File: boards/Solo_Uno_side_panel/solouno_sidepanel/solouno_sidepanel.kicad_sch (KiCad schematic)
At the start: 1 part, among them J1 Conn_01x02

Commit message: Add files via upload
Updated Solo uno board
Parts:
- added A1: Aviation Connector, Library:GX-16-3, symbol Connector:DIN-3
- added A2: Aviation Pin, Connector_PinHeader_2.54mm:PinHeader_1x03_P2.54mm_Vertical, symbol Connector_Generic:Conn_01x03
- added C1: 3.3uF, Capacitor_THT:CP_Radial_D4.0mm_P1.50mm, symbol Device:C
- added CN1: CAN Front, Connector_PinHeader_2.54mm:PinHeader_1x02_P2.54mm_Vertical, symbol Connector_Generic:Conn_01x02
- added CN2: CAN Back, Connector_PinHeader_2.54mm:PinHeader_1x02_P2.54mm_Vertical, symbol Connector_Generic:Conn_01x02
- added E1: Encoder Front, Connector_PinHeader_2.54mm:PinHeader_1x05_P2.54mm_Vertical, symbol Connector_Generic:Conn_01x05
- added E2: Encoder Back, Connector_PinHeader_2.54mm:PinHeader_1x05_P2.54mm_Vertical, symbol Connector_Generic:Conn_01x05
- added PW2: Power Back, Connector_PinHeader_2.54mm:PinHeader_1x02_P2.54mm_Vertical, symbol Connector_Generic:Conn_01x02
- added S1: Pin, Connector_Wire:SolderWire-0.5sqmm_1x04_P4.6mm_D0.9mm_OD2.1mm, symbol Connector:Conn_01x04_Pin
- PW1: renamed from J1; value Conn_01x02 -> Power Front; footprint (none) -> Connector_PinHeader_2.54mm:PinHeader_1x02_P2.54mm_Vertical
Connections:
- net +28V: now also S1.1 (Pin_1)
- net GND: now also S1.2 (Pin_2)
- new net: C1.1, PW2.1 (Pin_1)
- new net: PW2.2 (Pin_2), S1.4 (Pin_4)
- new net: E1.1 (Pin_1), E2.1 (Pin_1)
- new net: E1.2 (Pin_2), E2.2 (Pin_2)
- new net: E1.3 (Pin_3), E2.3 (Pin_3)
- new net: E1.4 (Pin_4), E2.4 (Pin_4)
- new net: E1.5 (Pin_5), E2.5 (Pin_5)
- new net: A1.1, A2.1 (Pin_1)
- new net: A1.2, A2.2 (Pin_2)
- new net: A1.3, A2.3 (Pin_3)
- new net: C1.2, S1.3 (Pin_3)
- new net: CN1.1 (Pin_1), CN2.1 (Pin_1)
- new net: CN1.2 (Pin_2), CN2.2 (Pin_2)
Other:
- moved on the sheet: PW1

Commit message: Updated Solon
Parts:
- A2: footprint Connector_PinHeader_2.54mm:PinHeader_1x03_P2.54mm_Vertical -> Connector_JST:JST_EH_B3B-EH-A_1x03_P2.50mm_Vertical
- C1: footprint Capacitor_THT:CP_Radial_D4.0mm_P1.50mm -> Capacitor_THT:C_Rect_L4.0mm_W2.5mm_P2.50mm
- CN1, CN2, PW1, PW2: footprint Connector_PinHeader_2.54mm:PinHeader_1x02_P2.54mm_Vertical -> Connector_JST:JST_EH_B2B-EH-A_1x02_P2.50mm_Vertical
- E1, E2: footprint Connector_PinHeader_2.54mm:PinHeader_1x05_P2.54mm_Vertical -> Connector_JST:JST_EH_B5B-EH-A_1x05_P2.50mm_Vertical
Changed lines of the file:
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@@
 			)
 		)
-		(property "Footprint" "Connector_PinHeader_2.54mm:PinHeader_1x02_P2.54mm_Vertical"
+		(property "Footprint" "Connector_JST:JST_EH_B2B-EH-A_1x02_P2.50mm_Vertical"
 			(at 99.06 64.77 0)
 			(effects
@@
 			)
 		)
-		(property "Footprint" "Connector_PinHeader_2.54mm:PinHeader_1x02_P2.54mm_Vertical"
+		(property "Footprint" "Connector_JST:JST_EH_B2B-EH-A_1x02_P2.50mm_Vertical"
 			(at 88.9 85.09 0)
 			(effects
@@
 			)
 		)
-		(property "Footprint" "Connector_PinHeader_2.54mm:PinHeader_1x05_P2.54mm_Vertical"
+		(property "Footprint" "Connector_JST:JST_EH_B5B-EH-A_1x05_P2.50mm_Vertical"
 			(at 123.19 64.77 0)
 			(effects
@@
 			)
 		)
-		(property "Footprint" "Connector_PinHeader_2.54mm:PinHeader_1x05_P2.54mm_Vertical"
+		(property "Footprint" "Connector_JST:JST_EH_B5B-EH-A_1x05_P2.50mm_Vertical"
 			(at 138.43 64.77 0)
 			(effects
@@
 			)
 		)
-		(property "Footprint" "Connector_PinHeader_2.54mm:PinHeader_1x03_P2.54mm_Vertical"
+		(property "Footprint" "Connector_JST:JST_EH_B3B-EH-A_1x03_P2.50mm_Vertical"
 			(at 69.85 54.61 0)
 			(effects
@@
 			)
 		)
-		(property "Footprint" "Capacitor_THT:CP_Radial_D4.0mm_P1.50mm"
+		(property "Footprint" "Capacitor_THT:C_Rect_L4.0mm_W2.5mm_P2.50mm"
 			(at 96.52 76.5048 0)
 			(effects
@@
 			)
 		)
-		(property "Footprint" "Connector_PinHeader_2.54mm:PinHeader_1x02_P2.54mm_Vertical"
+		(property "Footprint" "Connector_JST:JST_EH_B2B-EH-A_1x02_P2.50mm_Vertical"
 			(at 91.44 95.25 0)
 			(effects
@@
 			)
 		)
-		(property "Footprint" "Connector_PinHeader_2.54mm:PinHeader_1x02_P2.54mm_Vertical"
+		(property "Footprint" "Connector_JST:JST_EH_B2B-EH-A_1x02_P2.50mm_Vertical"
 			(at 106.68 95.25 0)
 			(effects

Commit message: side panel with Gerber
waiting for final aviation dimensions
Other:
- moved on the sheet: CN1, CN2
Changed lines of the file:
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@@
 	(wire
 		(pts
-			(xy 96.52 95.25) (xy 101.6 95.25)
+			(xy 138.43 106.68) (xy 143.51 106.68)
 		)
 		(stroke
@@
 	(wire
 		(pts
-			(xy 96.52 97.79) (xy 101.6 97.79)
+			(xy 138.43 109.22) (xy 143.51 109.22)
 		)
 		(stroke
@@
 		)
 		(property "Description" "3-pin DIN connector"
-			(at 69.85 72.39 0)
+			(at 68.58 80.264 0)
 			(effects
 				(font
@@
 	(symbol
 		(lib_id "Connector_Generic:Conn_01x02")
-		(at 91.44 95.25 0)
+		(at 133.35 106.68 0)
 		(mirror y)
 		(unit 1)
@@
 		(dnp no)
 		(property "Reference" "CN1"
-			(at 88.9 95.2499 0)
+			(at 130.81 106.6799 0)
 			(effects
 				(font
@@
 		)
 		(property "Value" "CAN Front"
-			(at 88.9 97.7899 0)
+			(at 130.81 109.2199 0)
 			(effects
 				(font
@@
 		)
 		(property "Footprint" "Connector_JST:JST_EH_B2B-EH-A_1x02_P2.50mm_Vertical"
-			(at 91.44 95.25 0)
+			(at 133.35 106.68 0)
 			(effects
 				(font
@@
 		)
 		(property "Datasheet" "~"
-			(at 91.44 95.25 0)
+			(at 133.35 106.68 0)
 			(effects
 				(font
@@
 		)
 		(property "Description" "Generic connector, single row, 01x02, script generated (kicad-library-utils/schlib/autogen/connector/)"
-			(at 91.44 95.25 0)
+			(at 133.35 106.68 0)
 			(effects
 				(font
@@
 	(symbol
 		(lib_id "Connector_Generic:Conn_01x02")
-		(at 106.68 95.25 0)
+		(at 148.59 106.68 0)
 		(unit 1)
 		(exclude_from_sim no)
@@
 		(fields_autoplaced yes)
 		(property "Reference" "CN2"
-			(at 109.22 95.2499 0)
+			(at 151.13 106.6799 0)
 			(effects
 				(font
@@
 		)
 		(property "Value" "CAN Back"
-			(at 109.22 97.7899 0)
+			(at 151.13 109.2199 0)
 			(effects
 				(font
@@
 		)
 		(property "Footprint" "Connector_JST:JST_EH_B2B-EH-A_1x02_P2.50mm_Vertical"
-			(at 106.68 95.25 0)
+			(at 148.59 106.68 0)
 			(effects
 				(font
@@
 		)
 		(property "Datasheet" "~"
-			(at 106.68 95.25 0)
+			(at 148.59 106.68 0)
 			(effects
 				(font
@@
 		)
 		(property "Description" "Generic connector, single row, 01x02, script generated (kicad-library-utils/schlib/autogen/connector/)"
-			(at 106.68 95.25 0)
-			(effects
-				(font
+			(at 148.59 106.68 0)
+			(effects
+				(font

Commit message: side panel
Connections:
- net GND: now also C1.2, PW2.2 (Pin_2), S1.4 (Pin_4)
- net at C1.1, PW2.1 (Pin_1): now also S1.3 (Pin_3)
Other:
- moved on the sheet: C1, CN1, CN2, E1, E2, PW2

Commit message: updated solouno with new footprint
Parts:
- A1: footprint Library:GX-16-3 -> Connector:GX-16-3
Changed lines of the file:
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@@
 			)
 		)
-		(property "Footprint" "Library:GX-16-3"
+		(property "Footprint" "Connector:GX-16-3"
 			(at 69.85 72.39 0)
 			(effects

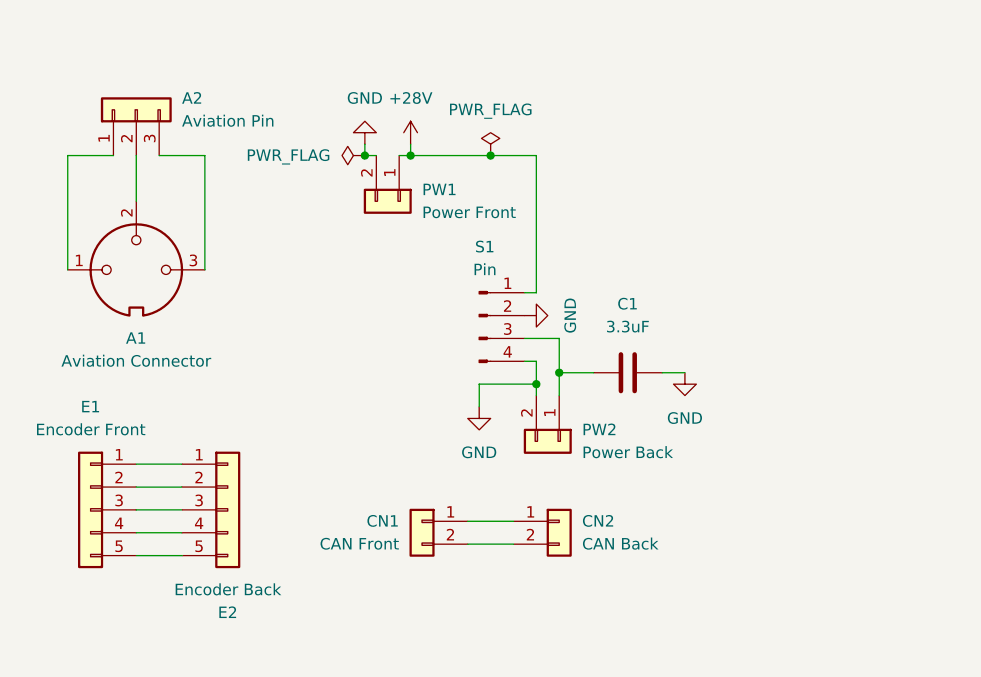
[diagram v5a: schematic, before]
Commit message: updated Solouno
Two pin for rocker switch
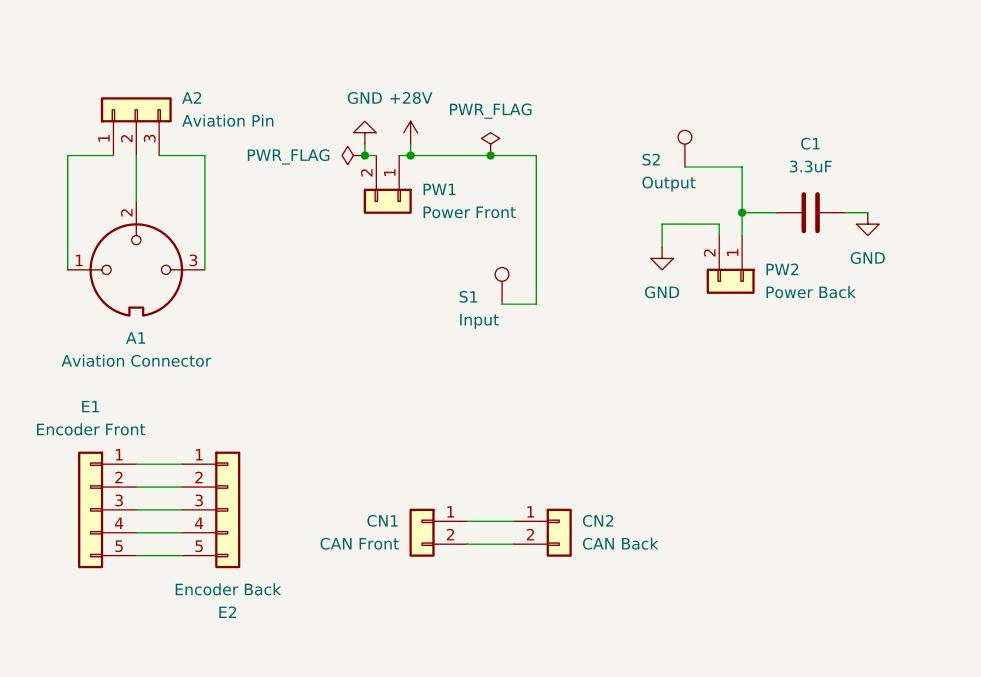
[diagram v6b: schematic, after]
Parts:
- removed S1: Pin, Connector_Wire:SolderWire-0.5sqmm_1x04_P4.6mm_D0.9mm_OD2.1mm, symbol Connector:Conn_01x04_Pin
- added S1: Input, TestPoint:TestPoint_Pad_4.0x4.0mm, symbol Connector:TestPoint
- added S2: Output, TestPoint:TestPoint_Pad_4.0x4.0mm, symbol Connector:TestPoint
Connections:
- net +28V: now also S1.1
- net at C1.1, PW2.1 (Pin_1): now also S2.1
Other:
- moved on the sheet: C1, PW2

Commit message: solouno update
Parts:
- removed A2: Aviation Pin, Connector_JST:JST_EH_B3B-EH-A_1x03_P2.50mm_Vertical, symbol Connector_Generic:Conn_01x03
- removed C1: 3.3uF, Capacitor_THT:C_Rect_L4.0mm_W2.5mm_P2.50mm, symbol Device:C
- added T1: Test1, TestPoint:TestPoint_Pad_1.5x1.5mm, symbol Connector:TestPoint
- added T2: Test2, TestPoint:TestPoint_Pad_1.5x1.5mm, symbol Connector:TestPoint
- added T3: Test3, TestPoint:TestPoint_Pad_1.5x1.5mm, symbol Connector:TestPoint
- S1, S2: footprint TestPoint:TestPoint_Pad_4.0x4.0mm -> TestPoint:TestPoint_Loop_D3.50mm_Drill1.4mm_Beaded
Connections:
- net at A1.1: now also T1.1
- net at A1.2: now also T2.1
- net at A1.3: now also T3.1
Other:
- moved on the sheet: A1, CN1, CN2, E1, E2, PW1, PW2, S1, S2

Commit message: Fixed MotorController Board PCB and Footprint for Aviation Connector
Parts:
- A1: footprint Connector:GX-16-3 -> Robonav:GX-16-3
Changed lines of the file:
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@@
 			)
 		)
-		(property "Footprint" "Connector:GX-16-3"
+		(property "Footprint" "Robonav:GX-16-3"
 			(at 96.52 62.23 0)
 			(effects
@@
 		)
 		(instances
-			(project ""
+			(project "solouno_sidepanel"
 				(path "/fdb62d32-debd-41f2-861f-5e33af64510a"
 					(reference "S1")
